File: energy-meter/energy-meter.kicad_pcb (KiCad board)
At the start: 2 copper layers, 82 x 62.5 mm, 97 parts, among them J1 Screw_Terminal_01x04, J2 Conn_01x03, J3 I2C OLED Display, etc., K1 G5RL-U1A-E, P1 PineNut, T1 AP-2500, T2 BV 202 0154, U1 L9110S, U10 MCP6V96T-E/OT, U11 TS5A3159ADBVR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

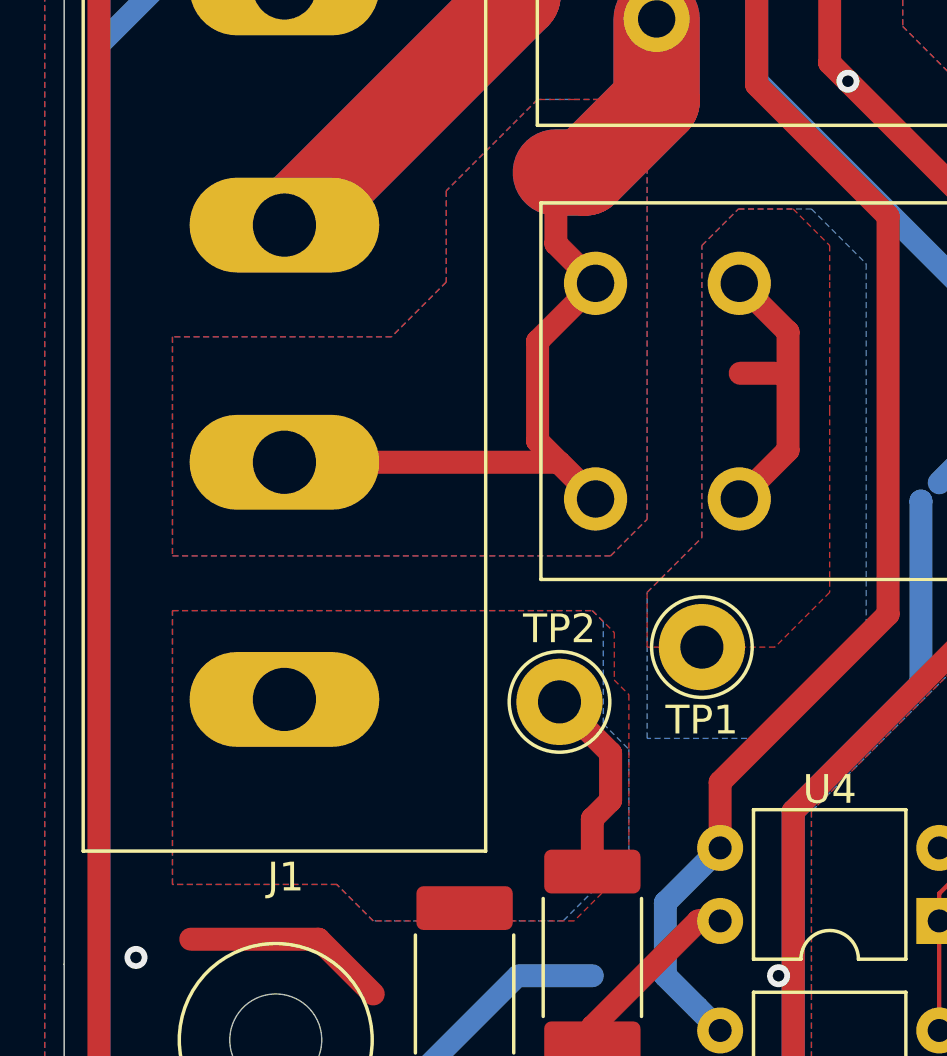
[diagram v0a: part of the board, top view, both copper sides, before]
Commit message: increase size of test points for wire through current transformer, unswap RELAY_SET/RESET
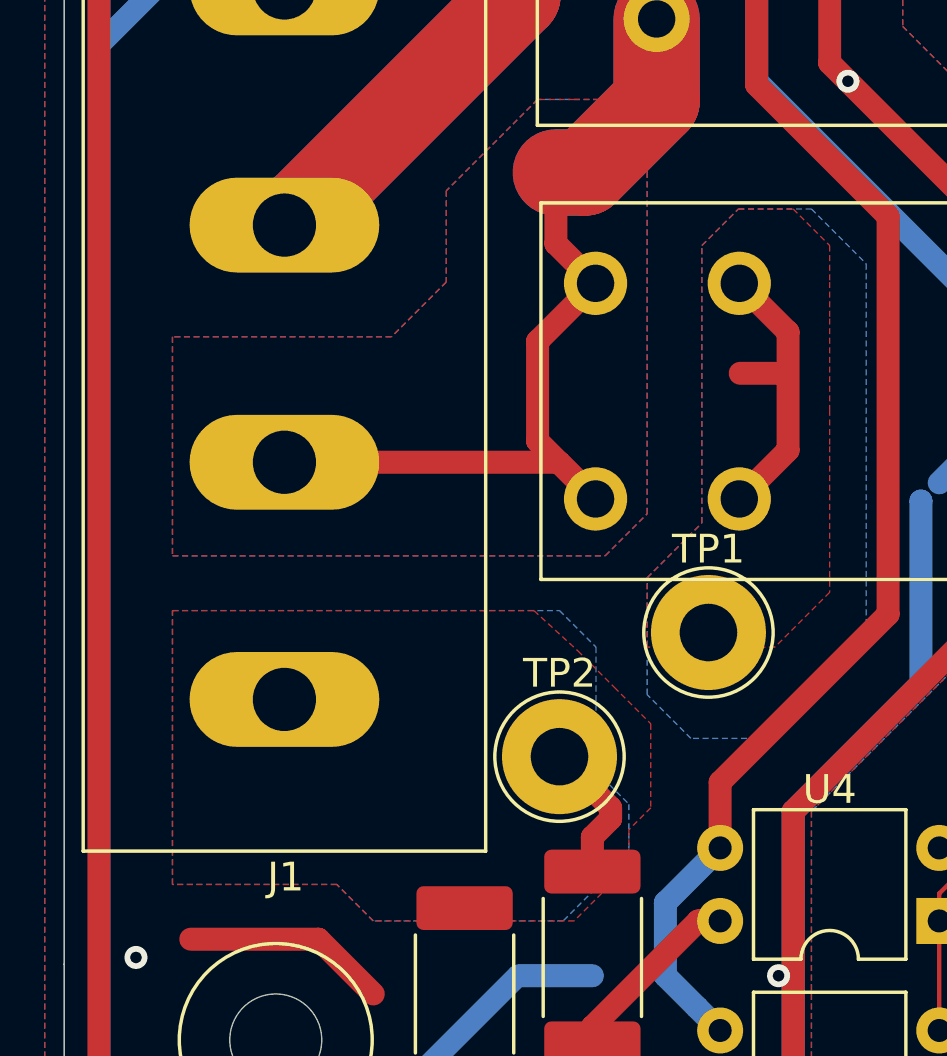
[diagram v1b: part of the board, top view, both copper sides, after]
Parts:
- TP1, TP2: footprint TestPoint:TestPoint_THTPad_D3.0mm_Drill1.5mm -> TestPoint:TestPoint_THTPad_D4.0mm_Drill2.0mm
- moved TP2 1.91 mm to (120.3, 139.2)
- moved TP1 0.56 mm to (125.5, 134.9)
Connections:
- R6 pad 2: /RELAY_SET -> /RELAY_RESET
- R7 pad 2: /RELAY_RESET -> /RELAY_SET
- U1 pad 6: /RELAY_RESET -> /RELAY_SET
- U1 pad 7: /RELAY_SET -> /RELAY_RESET
- U9 pad 11: /RELAY_SET -> /RELAY_RESET
- U9 pad 12: /RELAY_RESET -> /RELAY_SET
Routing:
- net L_OUT2: track 6.90 -> 5.00 mm

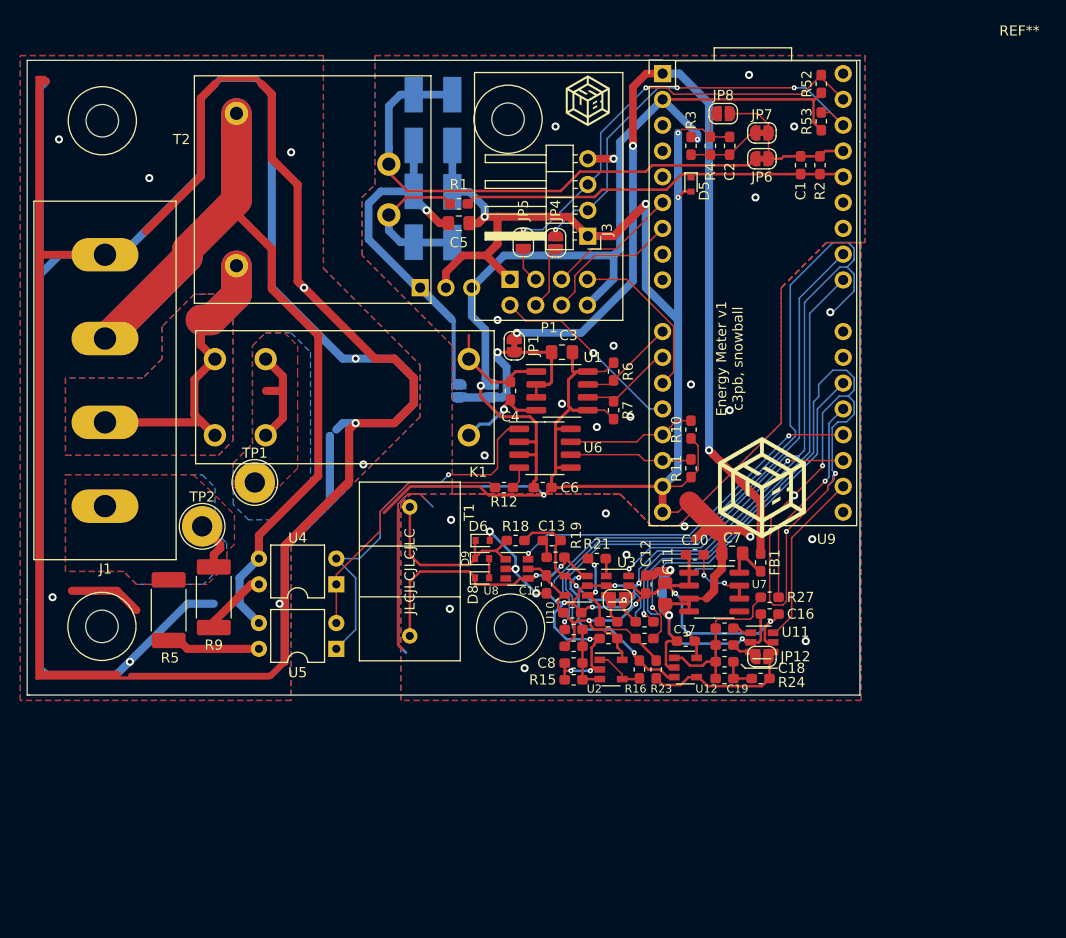
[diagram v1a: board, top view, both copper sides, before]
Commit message: handle most TODOs in schematic, PCB to be done
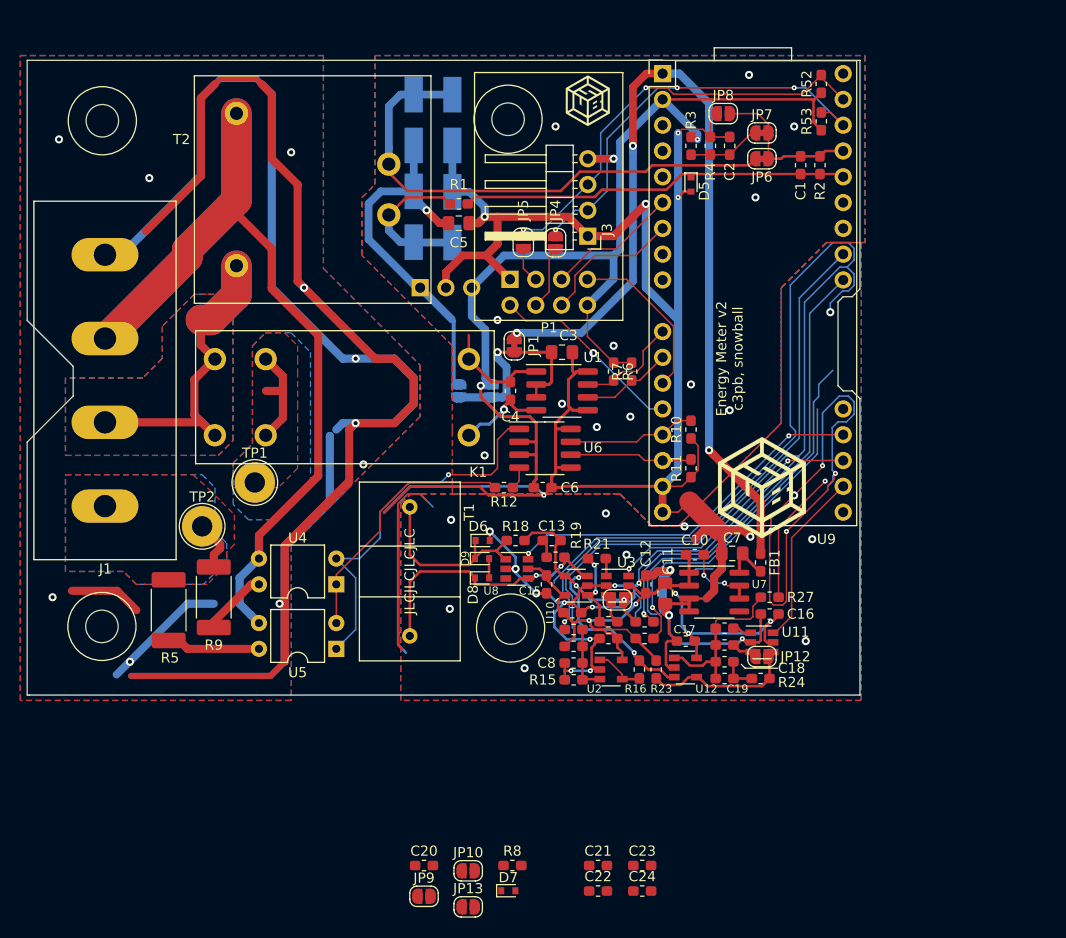
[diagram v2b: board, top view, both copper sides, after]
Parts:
- added C20: 10n, Capacitor_SMD:C_0603_1608Metric_Pad1.05x0.95mm_HandSolder, F.Cu at (142.1, 172.6)
- added C21: 12p, Capacitor_SMD:C_0603_1608Metric_Pad1.05x0.95mm_HandSolder, F.Cu at (159.3, 172.6)
- added C22: 12p, Capacitor_SMD:C_0603_1608Metric_Pad1.05x0.95mm_HandSolder, F.Cu at (159.3, 175.1)
- added C23: 470p, Capacitor_SMD:C_0603_1608Metric_Pad1.05x0.95mm_HandSolder, F.Cu at (163.6, 172.6)
- added C24: 470p, Capacitor_SMD:C_0603_1608Metric_Pad1.05x0.95mm_HandSolder, F.Cu at (163.6, 175.1)
- added D7: ESD5Z5.0T1G, Diode_SMD:D_SOD-523, F.Cu at (150.4, 175.1)
- added JP10: SolderJumper_2_Open, Jumper:SolderJumper-2_P1.3mm_Open_RoundedPad1.0x1.5mm, F.Cu at (146.5, 173.1)
- added JP13: SolderJumper_2_Open, Jumper:SolderJumper-2_P1.3mm_Open_RoundedPad1.0x1.5mm, F.Cu at (146.5, 176.7)
- added JP9: SolderJumper_2_Open, Jumper:SolderJumper-2_P1.3mm_Open_RoundedPad1.0x1.5mm, F.Cu at (142.1, 175.7)
- added R8: 10k, 0.1%, Resistor_SMD:R_0603_1608Metric_Pad1.05x0.95mm_HandSolder, F.Cu at (150.8, 172.6)
- C13: value 10n -> DNP / 6p
- R1: value 5k, 0.1% -> 10k, 0.1%
- R19: value 10R -> DNP / 10R
- R20: value 220R, 1% -> 200R, 1%
- R21: value 220k, 1% -> 10k, 1%
- moved R7 4.20 mm to (162.6, 124.0), turned to 270 degrees
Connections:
- R6 pad 1: GND -> +3V3
- R7 pad 1: GND -> +3V3
- U7 pad 5: Net-(U7-Pad5) -> /PGOOD
- U9 pad 23: /CURRENT_OUT1 -> /CURRENT_OUT0
- U9 pad 30: Net-(U9-Pad30) -> /CURRENT_OUT1
- U9 pad 31: Net-(U9-Pad31) -> /VOLTAGE1
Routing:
- net PE: track 475.4 -> 246.4 mm
- net +3V3: track 97.5 -> 106.0 mm
- net /CURRENT_OUT1: track 21.3 -> 13.5 mm
- net GND: track 188.5 -> 182.7 mm
- net GNDA: track 370.5 -> 366.3 mm
- net /CURRENT_OUT0: track 36.1 -> 32.5 mm
- net /RELAY_RESET: track 9.53 -> 10.4 mm
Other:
- outline, holes or cut-outs redrawn
- board text added: "Energy Meter v2 c3pb, snowball"
- board text removed: "Energy Meter v1 c3pb, snowball"

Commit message: fixups
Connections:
- C20 pad 1: /VOLTAGE1 -> /VOLTAGE1MCU
- D7 pad 1: /VOLTAGE1 -> /VOLTAGE1MCU
- R8 pad 2: /VOLTAGE1 -> /VOLTAGE1MCU
- U9 pad 31: /VOLTAGE1 -> /VOLTAGE1MCU

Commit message: old changes
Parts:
- added J4: SMA, Connector_Coaxial:SMA_Samtec_SMA-J-P-H-ST-EM1_EdgeMount, F.Cu at (157.8, 95.5)
- added J5: SMA, Connector_Coaxial:SMA_Samtec_SMA-J-P-H-ST-EM1_EdgeMount, F.Cu at (150.7, 153.7)
- added J6: SMA, Connector_Coaxial:SMA_Samtec_SMA-J-P-H-ST-EM1_EdgeMount, F.Cu at (180.9, 153.7)
- added JP14: SolderJumper_2_Open, Jumper:SolderJumper-2_P1.3mm_Open_RoundedPad1.0x1.5mm, F.Cu at (165.3, 141.9)
- added JP15: SolderJumper_2_Open, Jumper:SolderJumper-2_P1.3mm_Open_RoundedPad1.0x1.5mm, F.Cu at (159.7, 133.8)
- C5: value 10u -> DNP / 10u
- moved JP9 58.2 mm to (168.7, 123.9), turned to 180 degrees
- moved JP10 51.5 mm to (168.7, 126.6), turned to 180 degrees
- moved JP13 10.6 mm to (155.0, 170.3)
- moved U4 0.38 mm to (133.5, 145.3)
- moved U5 0.38 mm to (133.5, 151.7)
- renumbered REF** to H1, REF** to H2, REF** to H3, REF** to H4
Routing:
- net PE: track 246.4 -> 237.3 mm
- net N: track 104.2 -> 105.8 mm
- net L_IN: track 39.7 -> 40.6 mm
